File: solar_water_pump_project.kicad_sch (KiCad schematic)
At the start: 8 parts, among them J1 USB_C_Receptacle_USB2.0_16P, U1 NCP1117-3.3_SOT223, U2 RP2040, U3 ATA00A18S-L

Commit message: Updated MCU
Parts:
- added C3: C, symbol Device:C
- added R3, R4: 27.4, symbol Device:R
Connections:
- net UBS_D+ is gone; now on net USB_D+: J1.A6 (D+), J1.B6 (D+)
- net USB_D+: now also R3.1; no longer U2.47 (USB_DP)
- net USB_D-: now also R4.1; no longer U2.46 (USB_DM)
- net RUN: now reaches U2.26 (RUN)
- new net: R4.2, U2.46 (USB_DM)
- new net: R3.2, U2.47 (USB_DP)
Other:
- note added: "Make sure R3 and R4 are close to RP2040"
- moved on the sheet: U2
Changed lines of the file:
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@@
   (no_connect (at 309.88 62.23))
   (no_connect (at 309.88 64.77))
+  (wire (pts (xy 115.57 144.78) (xy 115.57 149.86))
+    (stroke (width 0) (type default))
+  )
   (wire (pts (xy 309.88 52.07) (xy 312.42 52.07))
     (stroke (width 0) (type default))
@@
     (stroke (width 0) (type default))
   )
+  (wire (pts (xy 115.57 154.94) (xy 115.57 152.4))
+    (stroke (width 0) (type default))
+  )
   (wire (pts (xy 342.9 44.45) (xy 342.9 45.72))
     (stroke (width 0) (type default))
   )
-  (wire (pts (xy 50.8 142.24) (xy 50.8 152.4))
+  (wire (pts (xy 132.08 218.44) (xy 132.08 228.6))
     (stroke (width 0) (type default))
   )
@@
     (stroke (width 0) (type default))
   )
+  (wire (pts (xy 124.46 142.24) (xy 132.08 142.24))
+    (stroke (width 0) (type default))
+  )
   (wire (pts (xy 309.88 39.37) (xy 316.23 39.37))
     (stroke (width 0) (type default))
   )
+  (wire (pts (xy 115.57 152.4) (xy 132.08 152.4))
+    (stroke (width 0) (type default))
+  )
   (wire (pts (xy 312.42 49.53) (xy 313.69 49.53))
     (stroke (width 0) (type default))
@@
     (stroke (width 0) (type default))
   )
-  (wire (pts (xy 76.2 149.86) (xy 76.2 152.4))
+  (wire (pts (xy 157.48 226.06) (xy 157.48 228.6))
+    (stroke (width 0) (type default))
+  )
+  (wire (pts (xy 113.03 144.78) (xy 115.57 144.78))
     (stroke (width 0) (type default))
   )
@@
     (stroke (width 0) (type default))
   )
-  (wire (pts (xy 39.37 76.2) (xy 50.8 76.2))
-    (stroke (width 0) (type default))
-  )
-  (wire (pts (xy 39.37 73.66) (xy 50.8 73.66))
+  (wire (pts (xy 93.98 154.94) (xy 105.41 154.94))
+    (stroke (width 0) (type default))
+  )
+  (wire (pts (xy 93.98 144.78) (xy 105.41 144.78))
     (stroke (width 0) (type default))
   )
@@
     (stroke (width 0) (type default))
   )
+  (wire (pts (xy 115.57 149.86) (xy 132.08 149.86))
+    (stroke (width 0) (type default))
+  )
   (wire (pts (xy 327.66 39.37) (xy 327.66 41.91))
     (stroke (width 0) (type default))
@@
     (stroke (width 0) (type default))
   )
-  (text "RP2040\n" (at 63.5 113.03 0)
+  (wire (pts (xy 113.03 154.94) (xy 115.57 154.94))
+    (stroke (width 0) (type default))
+  )
+  (text "RP2040\n" (at 144.78 189.23 0)
     (effects (font (size 4 4)) (justify left bottom))
   )
@@
     (effects (font (size 2 2)) (justify left bottom))
   )
+  (text "Make sure R3 and R4 are close to RP2040" (at 62.23 149.86 0)
+    (effects (font (size 1.27 1.27)) (justify left bottom))
+  )
+  (label "RUN" (at 124.46 142.24 0) (fields_autoplaced)
+    (effects (font (size 1.27 1.27)) (justify left bottom))
+  )
   (label "USB_D-" (at 313.69 49.53 0) (fields_autoplaced)
     (effects (font (size 1.27 1.27)) (justify left bottom))
   )
-  (label "USB_D+" (at 39.37 73.66 0) (fields_autoplaced)
+  (label "USB_D+" (at 93.98 144.78 0) (fields_autoplaced)
     (effects (font (size 1.27 1.27)) (justify left bottom))
   )
-  (label "USB_D-" (at 39.37 76.2 0) (fields_autoplaced)
+  (label "USB_D-" (at 93.98 154.94 0) (fields_autoplaced)
     (effects (font (size 1.27 1.27)) (justify left bottom))
   )
-  (label "UBS_D+" (at 313.69 54.61 0) (fields_autoplaced)
+  (label "USB_D+" (at 313.69 54.61 0) (fields_autoplaced)
     (effects (font (size 1.27 1.27)) (justify left bottom))
   )
-  (symbol (lib_id "power:GND") (at 76.2 152.4 0) (unit 1)
-    (in_bom yes) (on_board yes) (dnp no) (fields_autoplaced)
-    (property "Reference" "#PWR01" (at 76.2 158.75 0)
-      (effects (font (size 1.27 1.27)) hide)
-    )
-    (property "Value" "GND" (at 76.2 157.48 0)
-      (effects (font (size 1.27 1.27)))
-    )
-    (property "Footprint" "" (at 76.2 152.4 0)
-      (effects (font (size 1.27 1.27)) hide)
-    )
-    (property "Datasheet" "" (at 76.2 152.4 0)
+  (symbol (lib_id "Device:C") (at 190.5 120.65 0) (unit 1)
+    (in_bom yes) (on_board yes) (dnp no) (fields_autoplaced)
+    (property "Reference" "C3" (at 194.31 119.38 0)
+      (effects (font (size 1.27 1.27)) (justify left))
+    )
+    (property "Value" "C" (at 194.31 121.92 0)
+      (effects (font (size 1.27 1.27)) (justify left))
+    )
+    (property "Footprint" "" (at 191.4652 124.46 0)
+      (effects (font (size 1.27 1.27)) hide)
+    )
+    (property "Datasheet" "~" (at 190.5 120.65 0)
+      (effects (font (size 1.27 1.27)) hide)
+    )
+    (pin "2")
+    (pin "1")
+    (instances
+      (project "solar_water_pump_project"
+        (path "/b825e78c-745a-4fc2-8cc9-f01d0802d2de"
+          (reference "C3") (unit 1)
+        )
+      )
+    )
+  )
+  (symbol (lib_id "power:GND") (at 157.48 228.6 0) (unit 1)
+    (in_bom yes) (on_board yes) (dnp no) (fields_autoplaced)
+    (property "Reference" "#PWR01" (at 157.48 234.95 0)
+      (effects (font (size 1.27 1.27)) hide)
+    )
+    (property "Value" "GND" (at 157.48 233.68 0)
+      (effects (font (size 1.27 1.27)))
+    )
+    (property "Footprint" "" (at 157.48 228.6 0)
+      (effects (font (size 1.27 1.27)) hide)
+    )
+    (property "Datasheet" "" (at 157.48 228.6 0)
       (effects (font (size 1.27 1.27)) hide)
     )
@@
         (path "/b825e78c-745a-4fc2-8cc9-f01d0802d2de"
           (reference "#PWR01") (unit 1)
+        )
+      )
+    )
+  )
+  (symbol (lib_id "Device:R") (at 109.22 154.94 90) (unit 1)
+    (in_bom yes) (on_board yes) (dnp no) (fields_autoplaced)
+    (property "Reference" "R4" (at 109.22 148.59 90)
+      (effects (font (size 1.27 1.27)))
+    )
+    (property "Value" "27.4" (at 109.22 151.13 90)
+      (effects (font (size 1.27 1.27)))
+    )
+    (property "Footprint" "" (at 109.22 156.718 90)
+      (effects (font (size 1.27 1.27)) hide)
+    )
+    (property "Datasheet" "~" (at 109.22 154.94 0)
+      (effects (font (size 1.27 1.27)) hide)
+    )
+    (pin "2")
+    (pin "1")
+    (instances
+      (project "solar_water_pump_project"
+        (path "/b825e78c-745a-4fc2-8cc9-f01d0802d2de"
+          (reference "R4") (unit 1)
         )
       )
@@
     )
   )
-  (symbol (lib_id "power:GND") (at 50.8 152.4 0) (unit 1)
-    (in_bom yes) (on_board yes) (dnp no) (fields_autoplaced)
-    (property "Reference" "#PWR04" (at 50.8 158.75 0)
-      (effects (font (size 1.27 1.27)) hide)
-    )
-    (property "Value" "GND" (at 50.8 157.48 0)
-      (effects (font (size 1.27 1.27)))
-    )
-    (property "Footprint" "" (at 50.8 152.4 0)
-      (effects (font (size 1.27 1.27)) hide)
-    )
-    (property "Datasheet" "" (at 50.8 152.4 0)
+  (symbol (lib_id "power:GND") (at 132.08 228.6 0) (unit 1)
+    (in_bom yes) (on_board yes) (dnp no) (fields_autoplaced)
+    (property "Reference" "#PWR04" (at 132.08 234.95 0)
+      (effects (font (size 1.27 1.27)) hide)
+    )
+    (property "Value" "GND" (at 132.08 233.68 0)
+      (effects (font (size 1.27 1.27)))
+    )
+    (property "Footprint" "" (at 132.08 228.6 0)
+      (effects (font (size 1.27 1.27)) hide)
+    )
+    (property "Datasheet" "" (at 132.08 228.6 0)
       (effects (font (size 1.27 1.27)) hide)
     )
@@
     )
   )
-  (symbol (lib_id "MCU_RaspberryPi:RP2040") (at 76.2 104.14 0) (unit 1)
+  (symbol (lib_id "MCU_RaspberryPi:RP2040") (at 157.48 180.34 0) (unit 1)
     (in_bom yes) (on_board yes) (dnp no)
-    (property "Reference" "U2" (at 78.3941 148.59 0)
-      (effects (font (size 1.27 1.27)) (justify left))
-    )
-    (property "Value" "RP2040" (at 78.3941 151.13 0)
-      (effects (font (size 1.27 1.27)) (justify left))
-    )
-    (property "Footprint" "Package_DFN_QFN:QFN-56-1EP_7x7mm_P0.4mm_EP3.2x3.2mm" (at 76.2 104.14 0)
-      (effects (font (size 1.27 1.27)) hide)
-    )
-    (property "Datasheet" "https://datasheets.raspberrypi.com/rp2040/rp2040-datasheet.pdf" (at 76.2 104.14 0)
+    (property "Reference" "U2" (at 159.6741 224.79 0)
+      (effects (font (size 1.27 1.27)) (justify left))
+    )
+    (property "Value" "RP2040" (at 159.6741 227.33 0)
+      (effects (font (size 1.27 1.27)) (justify left))
+    )
+    (property "Footprint" "Package_DFN_QFN:QFN-56-1EP_7x7mm_P0.4mm_EP3.2x3.2mm" (at 157.48 180.34 0)
+      (effects (font (size 1.27 1.27)) hide)
+    )
+    (property "Datasheet" "https://datasheets.raspberrypi.com/rp2040/rp2040-datasheet.pdf" (at 157.48 180.34 0)
       (effects (font (size 1.27 1.27)) hide)
     )
@@
         )
       )
+    )
+  )
+  (symbol (lib_id "Device:R") (at 109.22 144.78 90) (unit 1)
+    (in_bom yes) (on_board yes) (dnp no) (fields_autoplaced)
+    (property "Reference" "R3" (at 109.22 138.43 90)
+      (effects (font (size 1.27 1.27)))
+    )
+    (property "Value" "27.4" (at 109.22 140.97 90)
+      (effects (font (size 1.27 1.27)))
+    )
+    (property "Footprint" "" (at 109.22 146.558 90)
+      (effects (font (size 1.27 1.27)) hide)
+    )
+    (property "Datasheet" "~" (at 109.22 144.78 0)
+      (effects (font (size 1.27 1.27)) hide)
+    )
+    (pin "2")
+    (pin "1")
+    (instances
+      (project "solar_water_pump_project"
+        (path "/b825e78c-745a-4fc2-8cc9-f01d0802d2de"
+          (reference "R3") (unit 1)
+        )
+      )

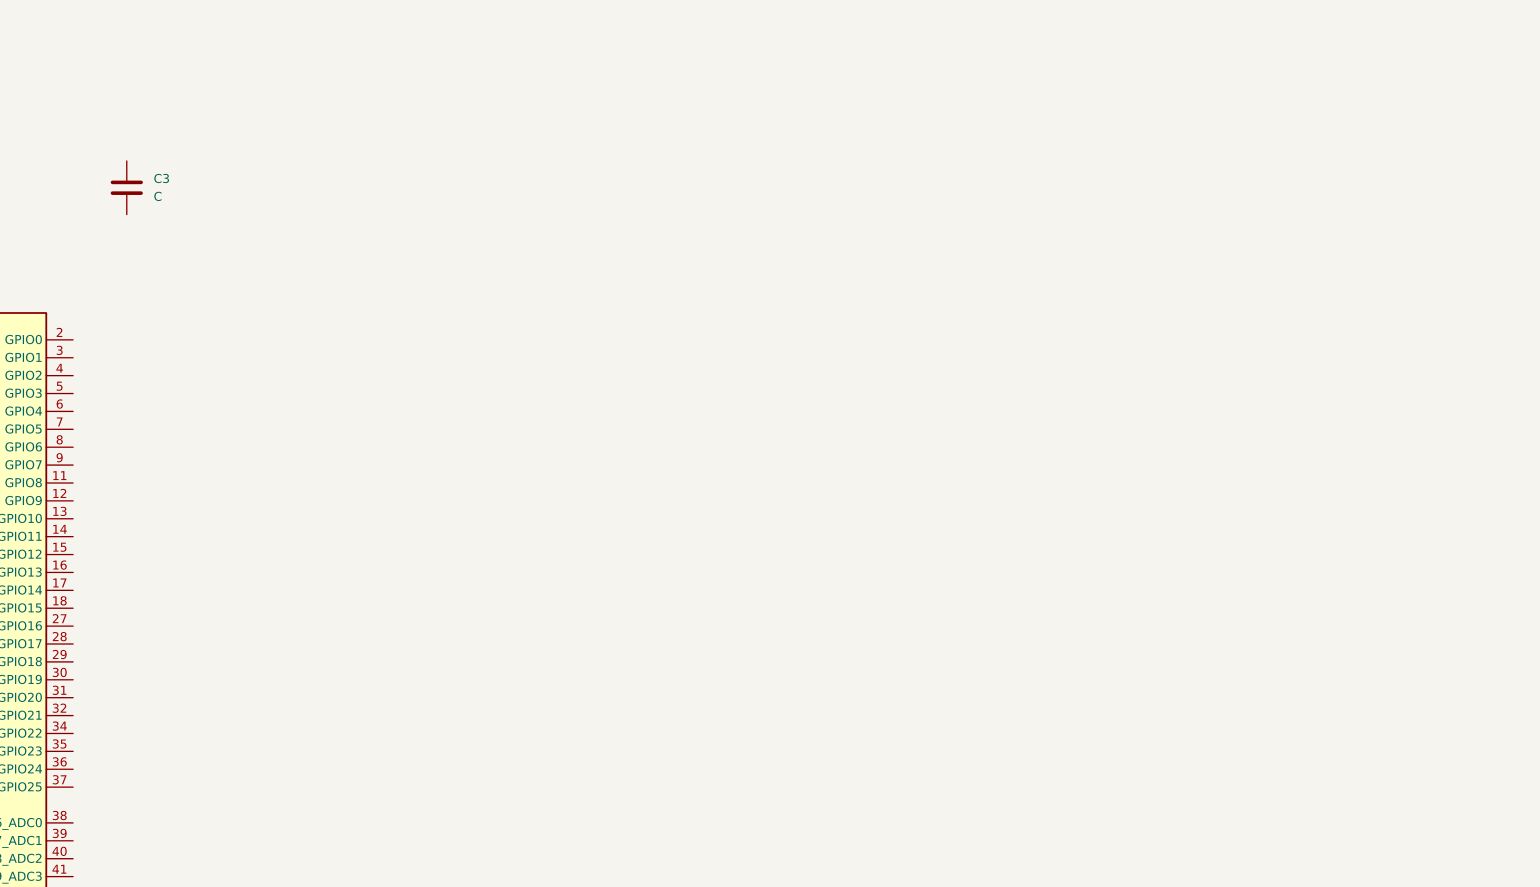
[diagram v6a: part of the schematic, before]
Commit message: Added LEDs and a horn, both still need work
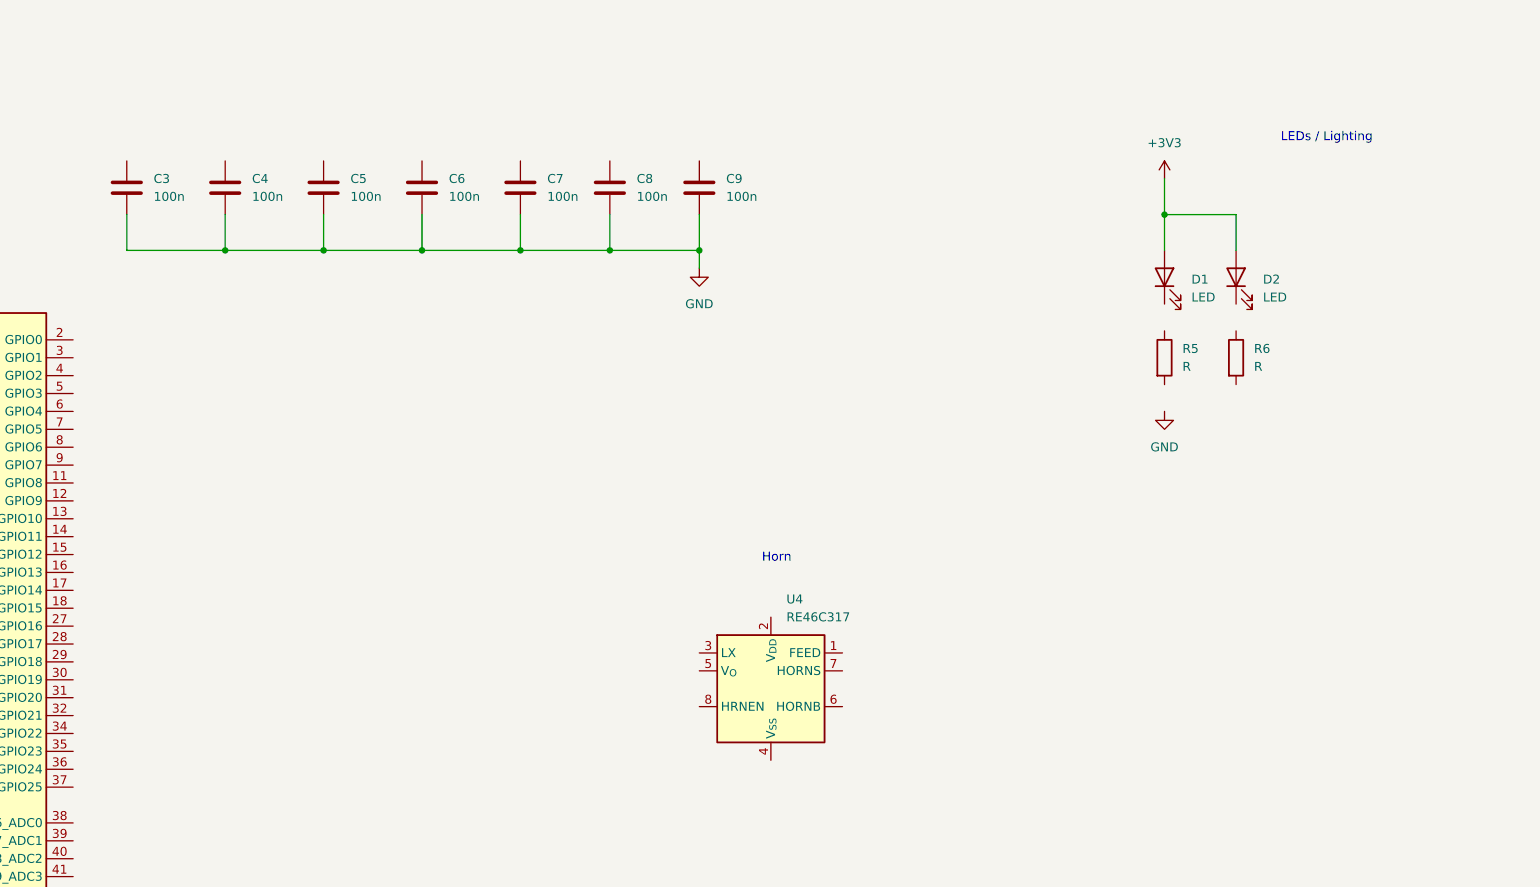
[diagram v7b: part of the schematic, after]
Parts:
- added C4, C5, C6, C7, C8, C9: 100n, symbol Device:C
- added D1, D2: LED, symbol Device:LED
- added R5, R6: R, symbol Device:R
- added U4: RE46C317, symbol Audio:RE46C317
- C3: value C -> 100n
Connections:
- net +3V3: now also D1.2 (A), D2.2 (A)
- net GND: now also C3.2, C4.2, C5.2, C6.2, C7.2, C8.2, C9.2
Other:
- note added: "Horn"
- note added: "LEDs / Lighting"

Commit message: changed LED
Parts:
- removed D2: LED, symbol Device:LED
- removed R6: R, symbol Device:R
- added Q1: NMOS, symbol Simulation_SPICE:NMOS
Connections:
- net +3V3: now also Q1.1 (D); no longer D1.2 (A)
- net GND: now also U4.4 (V_{SS})
- new net: D1.2 (A), Q1.3 (S)
- new net GPIO0: Q1.2 (G)
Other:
- note added: "LED"
- note removed: "LEDs / Lighting"
- moved on the sheet: C3, C4, C5, C6, C7, C8, C9, U4
